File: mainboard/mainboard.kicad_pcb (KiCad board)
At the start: 2 copper layers, 3 parts, among them U1 ESP32-WROOM-32, U2 tps63070, U3 tps63070

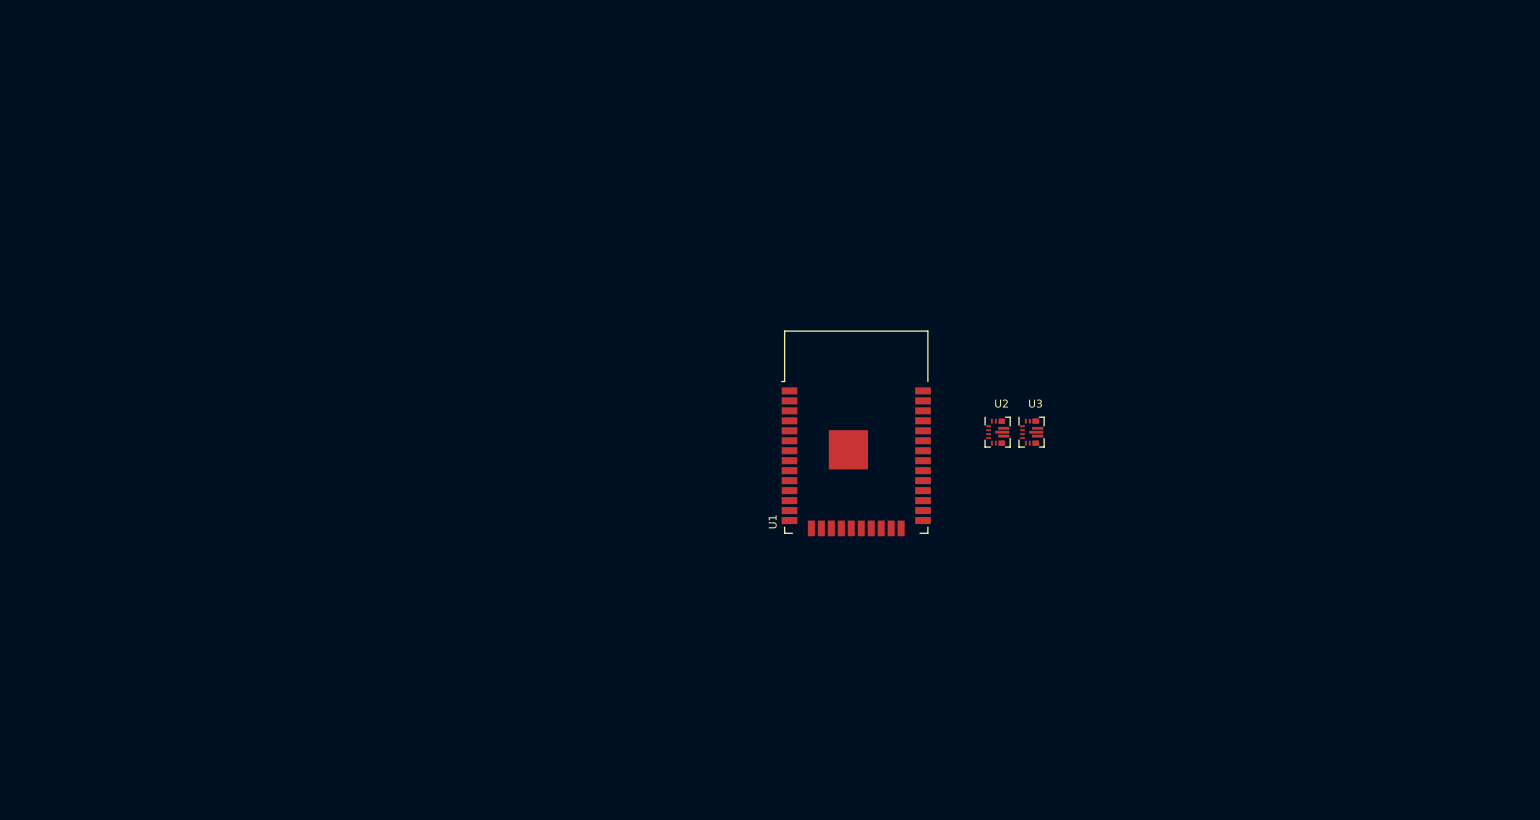
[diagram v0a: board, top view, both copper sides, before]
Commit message: Add sensors
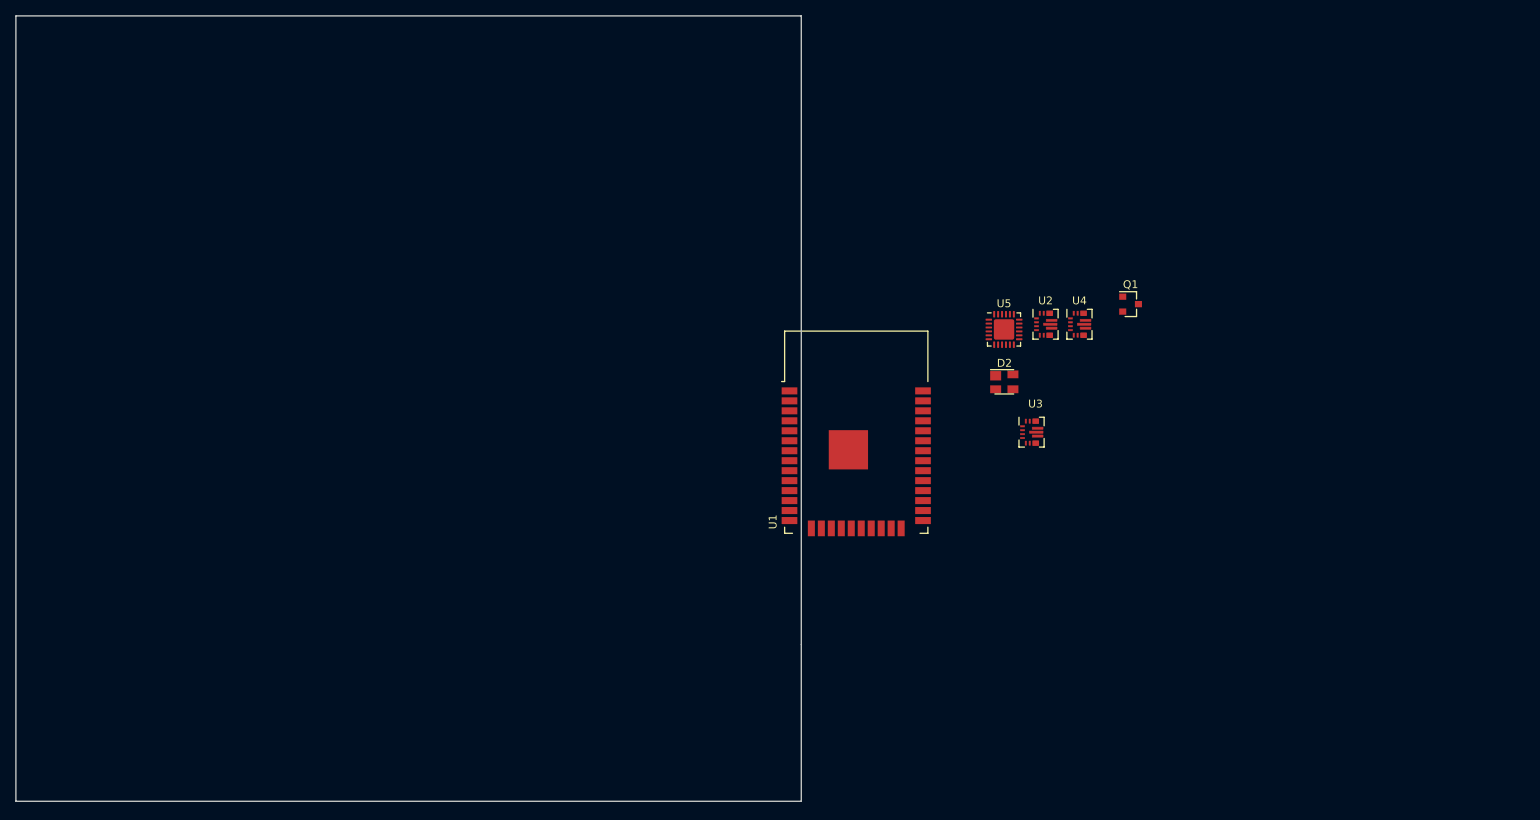
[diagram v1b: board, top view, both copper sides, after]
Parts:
- added D2: SP0503BAHT, Package_TO_SOT_SMD:SOT-143, F.Cu at (155.8, 76.6)
- added Q1: PMV32UP, Package_TO_SOT_SMD:SOT-23, F.Cu at (171.9, 66.7)
- added U4: tps63070, tps63070:VQFN-HR-15, F.Cu at (165.4, 69.3)
- added U5: CP2102N-A01-GQFN24, Package_DFN_QFN:QFN-24-1EP_4x4mm_P0.5mm_EP2.6x2.6mm, F.Cu at (155.8, 69.9)
- moved U2 15.0 mm to (161.1, 69.3)
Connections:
- net Net-(U1-Pad13) renamed /SCLK
- net Net-(U1-Pad14) renamed /SOUT1
- net Net-(U1-Pad16) renamed /SIN0
- net Net-(U1-Pad25) renamed /IO0
- net Net-(U1-Pad3) renamed /EN
- net Net-(U1-Pad35) renamed /TXD
- net Net-(U1-Pad8) renamed /GSCLK
- net Net-(U1-Pad9) renamed /LAT
- U1 pad 1: Net-(U1-Pad1) -> GND
- U1 pad 15: Net-(U1-Pad1) -> GND
- U1 pad 2: Net-(U1-Pad2) -> +3V3
- U1 pad 34: Net-(U1-Pad34) -> /RXD
- U1 pad 38: Net-(U1-Pad1) -> GND
- U2 pad 10: Net-(U2-Pad10) -> GND
- U2 pad 12: Net-(U2-Pad12) -> VBUS
- U2 pad 14: (no net) -> /VCC_EN
- U2 pad 15: Net-(U2-Pad15) -> GND
- U2 pad 2: (no net) -> /~PG_VCC0
- U2 pad 4: Net-(U2-Pad4) -> GND
- U2 pad 6: Net-(U2-Pad6) -> GND
- U3 pad 1: Net-(U3-Pad1) -> Net-(R1-Pad1)
- U3 pad 10: Net-(U3-Pad10) -> GND
- U3 pad 12: Net-(U3-Pad12) -> VBUS
- U3 pad 14: (no net) -> Net-(R1-Pad1)
- U3 pad 15: Net-(U3-Pad15) -> GND
- U3 pad 2: (no net) -> /~PG_3V3
- U3 pad 4: Net-(U3-Pad4) -> GND
- U3 pad 6: Net-(U3-Pad6) -> GND
- U3 pad 7: Net-(U3-Pad7) -> +3V3
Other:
- board outline added: 100 x 100 mm

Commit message: Layouting WIP
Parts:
- added C1: C, Capacitor_SMD:C_0805_2012Metric, F.Cu at (110.2, 119.5)
- added C10: 100 nC, Capacitor_SMD:C_0805_2012Metric, F.Cu at (105.1, 116.8)
- added C11: 100 nC, Capacitor_SMD:C_0805_2012Metric, F.Cu at (201.8, 83.7)
- added C12: 100 nC, Capacitor_SMD:C_0805_2012Metric, F.Cu at (196.2, 89.3)
- added C13: C, Capacitor_SMD:C_0603_1608Metric, F.Cu at (105.0, 122.0)
- added C14: C, Capacitor_SMD:C_0603_1608Metric, F.Cu at (214.1, 98.3)
- added C15: C, Capacitor_SMD:C_0603_1608Metric, F.Cu at (200.8, 107.1)
- added C16: C, Capacitor_SMD:C_0805_2012Metric, F.Cu at (104.0, 124.5)
- added C17: C, Capacitor_SMD:C_0805_2012Metric, F.Cu at (200.6, 89.6)
- added C18: C, Capacitor_SMD:C_0805_2012Metric, F.Cu at (183.4, 100.0)
- added C19: C, Capacitor_SMD:C_0805_2012Metric, F.Cu at (102.3, 121.0)
- added C2: C, Capacitor_SMD:C_0805_2012Metric, F.Cu at (206.2, 83.7)
- added C20: C, Capacitor_SMD:C_0805_2012Metric, F.Cu at (194.6, 97.4)
- added C21: C, Capacitor_SMD:C_0805_2012Metric, F.Cu at (187.8, 103.3)
- added C22: C, Capacitor_SMD:C_0805_2012Metric, F.Cu at (102.0, 124.5)
- added C23: C, Capacitor_SMD:C_0805_2012Metric, F.Cu at (199.0, 92.6)
- added C24: C, Capacitor_SMD:C_0805_2012Metric, F.Cu at (192.2, 100.4)
- added C25: C, Capacitor_SMD:C_0805_2012Metric, F.Cu at (206.2, 86.7)
- added C26: C, Capacitor_SMD:C_0805_2012Metric, F.Cu at (210.6, 83.7)
- added C27: C, Capacitor_SMD:C_0805_2012Metric, F.Cu at (187.8, 106.3)
- added C28: C, Capacitor_SMD:C_0805_2012Metric, F.Cu at (83.4, 122.3)
- added C29: C, Capacitor_SMD:C_0805_2012Metric, F.Cu at (76.6, 122.3)
- added C3: C, Capacitor_SMD:C_0805_2012Metric, F.Cu at (183.4, 106.0)
- added C30: C, Capacitor_SMD:C_0805_2012Metric, F.Cu at (83.4, 118.9)
- added C31: C, Capacitor_SMD:C_0805_2012Metric, F.Cu at (76.6, 118.9)
- added C32: C, Capacitor_SMD:C_0805_2012Metric, F.Cu at (196.6, 100.4)
- added C33: C, Capacitor_SMD:C_0805_2012Metric, F.Cu at (196.6, 106.3)
- added C34: C, Capacitor_SMD:C_0805_2012Metric, F.Cu at (215.0, 83.7)
- added C35: C, Capacitor_SMD:C_0805_2012Metric, F.Cu at (192.2, 106.3)
- added C36: 1 nC, Capacitor_SMD:C_0805_2012Metric, B.Cu at (72.2, 126.9)
- added C37: 1 nC, Capacitor_SMD:C_0805_2012Metric, B.Cu at (88.1, 126.9)
- added C38: 100 nC, Capacitor_SMD:C_0805_2012Metric, B.Cu at (69.4, 119.1)
- added C39: 1 uC, Capacitor_SMD:C_0805_2012Metric, F.Cu at (199.7, 65.2)
- added C4: C, Capacitor_SMD:C_0805_2012Metric, F.Cu at (110.6, 123.0)
- added C40: 100 nC, Capacitor_SMD:C_0805_2012Metric, F.Cu at (192.9, 72.9)
- added C41: 100 nC, Capacitor_SMD:C_0805_2012Metric, F.Cu at (65.6, 124.2)
- added C42: 100 nC, Capacitor_SMD:C_0805_2012Metric, F.Cu at (204.1, 65.2)
- added C43: 100 nC, Capacitor_SMD:C_0805_2012Metric, F.Cu at (197.3, 72.0)
- added C5: C, Capacitor_SMD:C_0805_2012Metric, F.Cu at (194.6, 94.5)
- added C6: C, Capacitor_SMD:C_0805_2012Metric, F.Cu at (183.4, 103.0)
- added C7: C, Capacitor_SMD:C_0603_1608Metric, F.Cu at (108.0, 122.0)
- added C8: C, Capacitor_SMD:C_0603_1608Metric, F.Cu at (209.7, 104.2)
- added C9: C, Capacitor_SMD:C_0603_1608Metric, F.Cu at (220.8, 92.4)
- added D1: PMEG3050EP,115, mainboard:SOD-128-2, F.Cu at (139.6, 48.9)
- added F1: Fuse, Fuse:Fuse_0805_2012Metric, F.Cu at (202.8, 68.2)
- added F2: Fuse, Fuse:Fuse_0805_2012Metric, F.Cu at (197.3, 75.0)
- added F3: Fuse, Fuse:Fuse_0805_2012Metric, F.Cu at (201.7, 72.0)
- added J1: USB_B_Micro, Connector_USB:USB_Micro-B_Amphenol_10103594-0001LF_Horizontal, F.Cu at (80.1, 127.1)
- added J2: Conn_01x19_MountingPin, mainboard:Molex_Easy-On_52746-1971_1x19_P0.5mm_Horizontal, F.Cu at (114.0, 88.0)
- added J3: Conn_01x19_MountingPin, mainboard:Molex_Easy-On_52746-1971_1x19_P0.5mm_Horizontal, F.Cu at (63.0, 87.0)
- added JP1: Jumper_3_Bridged12, Jumper:SolderJumper-3_P1.3mm_Bridged12_Pad1.0x1.5mm, B.Cu at (68.8, 127.5)
- added JP2: Jumper_3_Bridged12, Jumper:SolderJumper-3_P1.3mm_Bridged12_Pad1.0x1.5mm, B.Cu at (72.8, 118.8)
- added JP3: Jumper_3_Bridged12, Jumper:SolderJumper-3_P1.3mm_Bridged12_Pad1.0x1.5mm, B.Cu at (69.3, 123.2)
- added JP4: Jumper, Jumper:SolderJumper-2_P1.3mm_Bridged_Pad1.0x1.5mm, F.Cu at (206.1, 74.4)
- added L1: L, Inductor_SMD:L_Coilcraft_XxL4020, F.Cu at (107.3, 125.1)
- added L2: L, Inductor_SMD:L_Coilcraft_XxL4020, F.Cu at (179.6, 95.8)
- added L3: L, Inductor_SMD:L_Coilcraft_XxL4020, F.Cu at (185.2, 95.8)
- added Q2: MMBT3904, Package_TO_SOT_SMD:SOT-23, F.Cu at (73.5, 122.3)
- added Q3: MMBT3904, Package_TO_SOT_SMD:SOT-23, F.Cu at (86.5, 122.2)
- added R1: 10 kR, Resistor_SMD:R_0805_2012Metric, F.Cu at (112.2, 119.5)
- added R10: 10 kR, Resistor_SMD:R_0805_2012Metric, F.Cu at (108.7, 116.8)
- added R11: 10 kR, Resistor_SMD:R_0805_2012Metric, F.Cu at (160.1, 62.1)
- added R12: 10 kR, Resistor_SMD:R_0805_2012Metric, F.Cu at (164.5, 62.1)
- added R13: 2.2 kR, Resistor_SMD:R_0805_2012Metric, F.Cu at (201.7, 75.0)
- added R14: 2.2 kR, Resistor_SMD:R_0805_2012Metric, F.Cu at (206.1, 71.1)
- added R15: 100 kR, Resistor_SMD:R_0805_2012Metric, F.Cu at (212.2, 95.5)
- added R16: 1 kR, Resistor_SMD:R_0805_2012Metric, F.Cu at (218.3, 89.6)
- added R17: 4.7 kR, Resistor_SMD:R_0805_2012Metric, F.Cu at (80.0, 119.1)
- added R18: 470 R, Resistor_SMD:R_0805_2012Metric, B.Cu at (85.1, 119.3)
- added R19: 12 kR, Resistor_SMD:R_0805_2012Metric, B.Cu at (74.4, 122.3)
- added R2: 10 kR, Resistor_SMD:R_0805_2012Metric, F.Cu at (207.8, 92.6)
- added R20: 12 kR, Resistor_SMD:R_0805_2012Metric, B.Cu at (87.3, 122.2)
- added R21: 470 R, Resistor_SMD:R_0805_2012Metric, B.Cu at (74.4, 126.9)
- added R22: 470 R, Resistor_SMD:R_0805_2012Metric, B.Cu at (85.8, 126.9)
- added R3: 10 kR, Resistor_SMD:R_0805_2012Metric, F.Cu at (201.1, 98.5)
- added R4: 470 kR, Resistor_SMD:R_0805_2012Metric, F.Cu at (104.3, 119.5)
- added R5: 150 kR, Resistor_SMD:R_0805_2012Metric, F.Cu at (102.3, 117.5)
- added R6: 470 kR, Resistor_SMD:R_0805_2012Metric, F.Cu at (201.1, 101.4)
- added R7: 120 kR, Resistor_SMD:R_0805_2012Metric, F.Cu at (187.8, 100.4)
- added R8: 470 kR, Resistor_SMD:R_0805_2012Metric, F.Cu at (207.8, 95.5)
- added R9: 120 kR, Resistor_SMD:R_0805_2012Metric, F.Cu at (213.8, 89.6)
- added SW1: SW_Push, Button_Switch_SMD:SW_Push_SPST_NO_Alps_SKRK, F.Cu at (72.2, 127.0)
- added SW2: SW_Push, Button_Switch_SMD:SW_Push_SPST_NO_Alps_SKRK, F.Cu at (88.1, 126.9)
- added U6: BME680, Package_LGA:Bosch_LGA-8_3x3mm_P0.8mm_ClockwisePinNumbering, F.Cu at (69.4, 119.1)
- added U7: BH1750FVI, mainboard:WSOF6I, F.Cu at (68.7, 127.8)
- added U8: LIS3MDL, Package_LGA:LGA-12_2x2mm_P0.5mm, F.Cu at (68.9, 123.5)
- added U9: ADXL343, Package_LGA:LGA-14_3x5mm_P0.8mm_LayoutBorder1x6y, F.Cu at (93.9, 102.4)
- Q1: value PMV32UP -> DMG2301L
- U5: moved to B.Cu
- moved U5 91.1 mm to (80.0, 120.5), turned to 90 degrees
- moved D2 88.5 mm to (80.0, 122.1)
- moved U3 63.6 mm to (107.3, 119.6), turned to 270 degrees
- moved U1 60.3 mm to (80.0, 105.7)
- moved Q1 3.88 mm to (173.1, 63.0), turned to 90 degrees
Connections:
- Q1 pad 3: VDC -> Net-(F3-Pad1)
- U1 pad 10: Net-(U1-Pad10) -> /SCL
- U1 pad 11: Net-(U1-Pad11) -> /SDA
- U1 pad 12: Net-(U1-Pad12) -> /VCC1_EN
- U1 pad 14: /SOUT1 -> Net-(JP4-Pad1)
- U1 pad 27: Net-(U1-Pad27) -> /PG_VCC0
- U1 pad 28: Net-(U1-Pad28) -> /PG_VCC1
- U1 pad 30: Net-(U1-Pad30) -> /SCK
- U1 pad 31: Net-(U1-Pad31) -> /MISO
- U1 pad 33: Net-(U1-Pad33) -> /~CS_ACCEL
- U1 pad 36: Net-(U1-Pad36) -> /VCC0_EN
- U1 pad 37: Net-(U1-Pad37) -> /MOSI
- U1 pad 4: Net-(U1-Pad4) -> /DRDY
- U1 pad 5: Net-(U1-Pad5) -> /INT
- U1 pad 6: Net-(U1-Pad6) -> /INT1
- U1 pad 7: Net-(U1-Pad7) -> /INT2
- U2 pad 12: VBUS -> VDC
- U2 pad 14: /VCC_EN -> /VCC0_EN
- U2 pad 2: /~PG_VCC0 -> /PG_VCC0
- U2 pad 9: (no net) -> Net-(L2-Pad2)
- U3 pad 2: /~PG_3V3 -> /PG_3V3
- U3 pad 9: (no net) -> Net-(L1-Pad2)
- U4 pad 12: VBUS -> VDC
- U4 pad 14: /VCC_EN -> /VCC1_EN
- U4 pad 2: /~PG_VCC1 -> /PG_VCC1
- U4 pad 9: (no net) -> Net-(L3-Pad2)
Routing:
- net /EN: track 0.00 -> 28.6 mm, vias 0 -> 3
- net /RTS: track 0.00 -> 19.7 mm, vias 0 -> 1
- net /DTR: track 0.00 -> 18.5 mm, vias 0 -> 4
- net /IO0: track 0.00 -> 13.4 mm, vias 0 -> 1
- net Net-(C28-Pad1): track 0.00 -> 12.6 mm, vias 0 -> 1
- net VUSB: track 0.00 -> 12.1 mm, vias 0 -> 1
- net GND: track 0.00 -> 11.6 mm, vias 0 -> 9
- net Net-(R1-Pad1): track 0.00 -> 8.64 mm
- net +3V3: track 0.00 -> 8.36 mm, vias 0 -> 4
- net Net-(JP2-Pad2): track 0.00 -> 6.41 mm, vias 0 -> 1
- net Net-(R17-Pad1): track 0.00 -> 4.67 mm, vias 0 -> 1
- net Net-(R4-Pad1): track 0.00 -> 4.03 mm
- net /D+: track 0.00 -> 4.02 mm, vias 0 -> 1
- net /D-: track 0.00 -> 3.85 mm, vias 0 -> 1
- net Net-(C37-Pad2): track 0.00 -> 3.40 mm, vias 0 -> 1
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- added copper zone on F.Cu, net +3V3
- added copper zone on B.Cu, net GND
- added copper zone on F.Cu, net GND
- added copper zone on B.Cu, net Net-(L1-Pad1)
- added copper zone on B.Cu, net Net-(L1-Pad2)
- added copper zone on F.Cu, net VBUS
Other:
- outline, holes or cut-outs redrawn
- board text added: "BOOT"
- board text added: "EN"

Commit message: WIP
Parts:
- C1, C10, C13, C16, C19, C22, C4, C7, J2, J3, L1, R1, R10, R4, R5, U3, U9: moved to B.Cu
- moved U6 35.0 mm to (58.6, 85.8)
- moved C38 35.0 mm to (58.6, 85.8)
- moved JP2 35.0 mm to (62.0, 85.5)
- moved L1 32.9 mm to (79.7, 107.0)
- moved C22 32.3 mm to (74.4, 107.6), turned to 90 degrees
- moved C16 32.3 mm to (76.4, 107.6), turned to 90 degrees
- moved C4 30.8 mm to (83.0, 109.2), turned to 90 degrees
- moved C13 30.0 mm to (77.4, 110.1)
- moved C7 30.0 mm to (80.5, 110.1)
- moved C19 29.3 mm to (74.7, 111.1), turned to 270 degrees
- moved U3 28.4 mm to (79.7, 112.5), turned to 90 degrees
- moved C1 28.4 mm to (82.7, 112.6), turned to 270 degrees
- moved R1 28.4 mm to (84.7, 112.6), turned to 90 degrees
- moved R4 28.4 mm to (76.8, 112.6), turned to 90 degrees
- moved R5 27.7 mm to (74.8, 114.5), turned to 270 degrees
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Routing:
- net /EN: track 28.6 -> 3.07 mm, vias 3 -> 1
- net /IO0: track 13.4 -> 10.9 mm
- net +3V3: track 8.36 -> 10.5 mm
- net /PG_3V3: track 2.99 -> 1.75 mm
- net GND: vias 9 -> 10
- added copper zone on B.Cu, net +3V3
- added copper zone on F.Cu, net Net-(L1-Pad1)
- added copper zone on F.Cu, net Net-(L1-Pad2)
- added copper zone on B.Cu, net VBUS
- removed copper zone on F.Cu, net +3V3
- removed copper zone on B.Cu, net Net-(L1-Pad1)
- removed copper zone on B.Cu, net Net-(L1-Pad2)
- removed copper zone on F.Cu, net VBUS
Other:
- board size 100 x 100 mm -> 53 x 53 mm

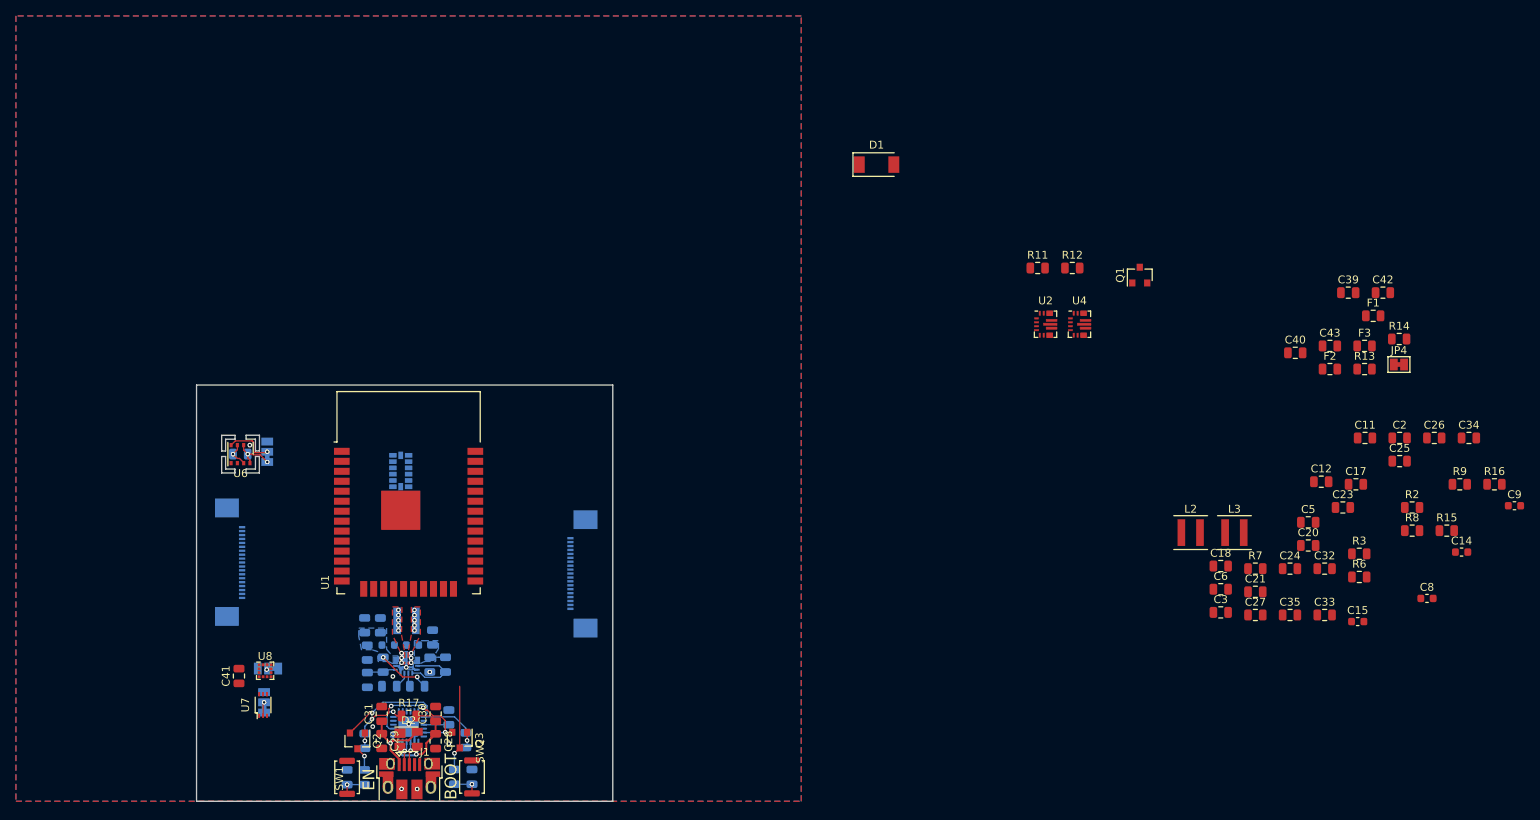
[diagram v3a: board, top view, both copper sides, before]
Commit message: Assemble regulator sections
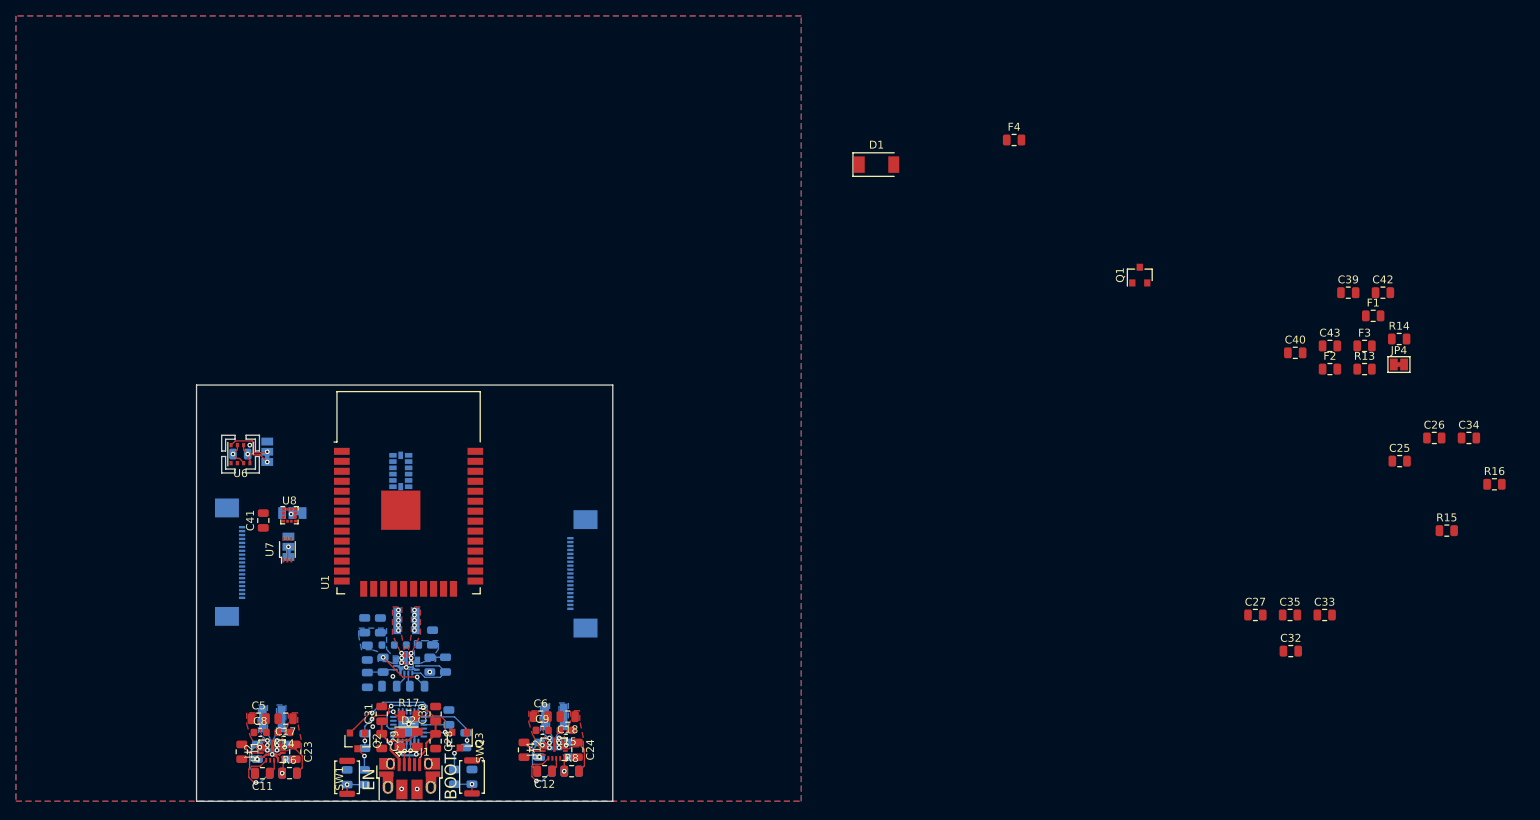
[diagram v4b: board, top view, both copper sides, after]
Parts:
- added F4: Fuse, Fuse:Fuse_0805_2012Metric, F.Cu at (157.1, 45.8)
- C2, C20, C21, C3, L2, L3, R2, R3, R7, R9: moved to B.Cu
- moved C14 151.7 mm to (64.1, 121.2), turned to 180 degrees
- moved C2 150.8 mm to (60.8, 123.7), turned to 270 degrees
- moved R2 150.3 mm to (61.4, 126.4), turned to 180 degrees
- moved C8 149.5 mm to (61.1, 121.2)
- moved C11 146.7 mm to (61.4, 126.4), turned to 180 degrees
- moved C17 139.5 mm to (64.3, 119.5), turned to 180 degrees
- moved R6 138.5 mm to (64.8, 126.4)
- moved C23 137.0 mm to (65.6, 123.7), turned to 270 degrees
- moved C5 136.0 mm to (60.9, 119.5)
- moved C20 132.7 mm to (64.5, 123.7), turned to 270 degrees
- moved C9 127.1 mm to (97.0, 121.0)
- moved R7 125.7 mm to (64.8, 126.4)
- moved L2 119.3 mm to (62.6, 119.5)
- moved R9 118.8 mm to (100.8, 126.2)
- moved R11 118.6 mm to (58.8, 123.7), turned to 270 degrees
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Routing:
- net VDC: track 0.00 -> 8.64 mm, vias 0 -> 2
- net /IO0: track 10.9 -> 3.02 mm
- net Net-(R2-Pad1): track 0.00 -> 7.15 mm, vias 0 -> 1
- net Net-(R3-Pad1): track 0.00 -> 7.14 mm, vias 0 -> 1
- net GND: track 11.6 -> 16.9 mm, vias 10 -> 13
- net Net-(C14-Pad1): track 0.00 -> 5.18 mm, vias 0 -> 1
- net Net-(C15-Pad1): track 0.00 -> 4.31 mm, vias 0 -> 1
- net /VCC0_EN: track 0.00 -> 2.92 mm
- net /VCC1_EN: track 0.00 -> 2.90 mm
- net Net-(R8-Pad1): track 0.00 -> 2.12 mm, vias 0 -> 1
- net Net-(R6-Pad1): track 0.00 -> 2.12 mm, vias 0 -> 1
- net Net-(C11-Pad1): track 0.00 -> 1.88 mm
- net Net-(C12-Pad1): track 0.00 -> 1.88 mm
- net Net-(L3-Pad2): vias 0 -> 3
- net Net-(L3-Pad1): vias 0 -> 3
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- added copper zone on F.Cu, net Net-(C14-Pad1)
- added copper zone on F.Cu, net Net-(C15-Pad1)
- added copper zone on B.Cu, net Net-(L2-Pad1)
- added copper zone on B.Cu, net Net-(L2-Pad2)
- added copper zone on B.Cu, net Net-(L3-Pad1)
- added copper zone on B.Cu, net Net-(L3-Pad2)
- added copper zone on F.Cu, net VDC
